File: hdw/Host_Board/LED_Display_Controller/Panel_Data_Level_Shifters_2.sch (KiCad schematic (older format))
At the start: 62 parts

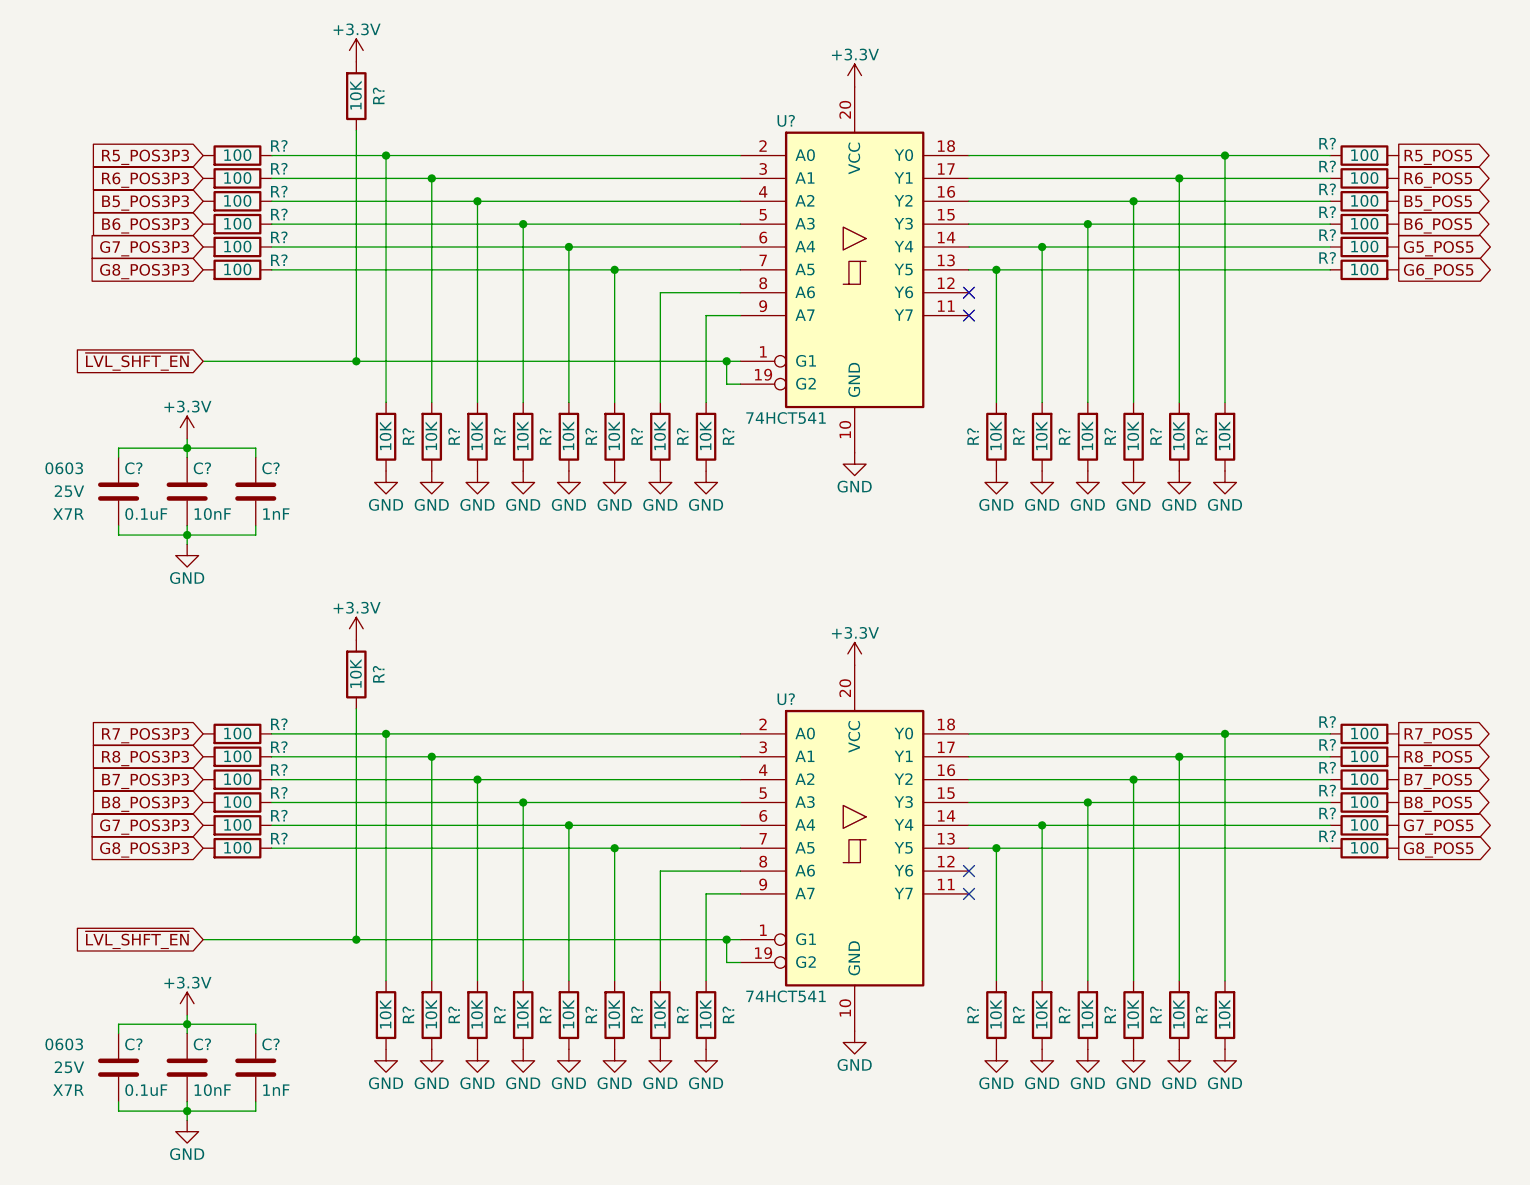
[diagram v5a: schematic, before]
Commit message: Added panel output enable AND gate
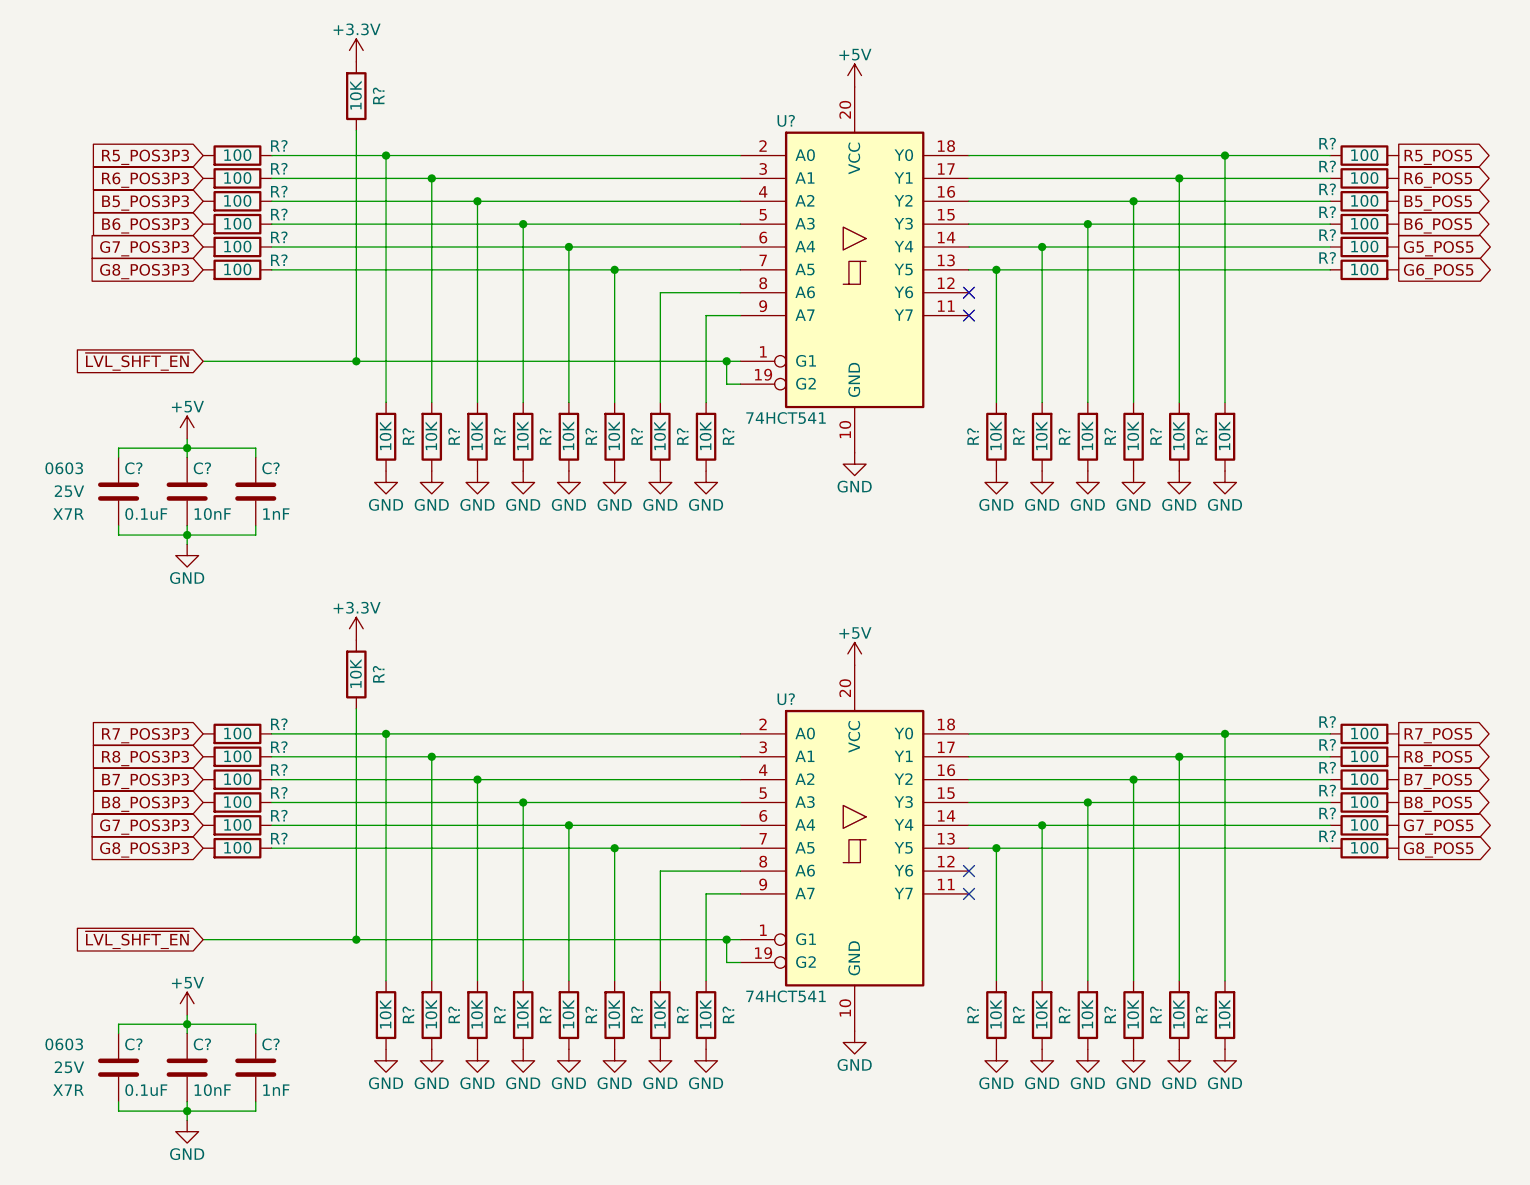
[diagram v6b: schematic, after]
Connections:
- net +3V3: no longer C?.1, C?.1, C?.1, C?.1, C?.1, C?.1, U?.20 (VCC), U?.20 (VCC)
- new net +5V: C?.1, C?.1, C?.1, C?.1, C?.1, C?.1, U?.20 (VCC), U?.20 (VCC)
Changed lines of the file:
@@
 $Descr A 11000 8500
 encoding utf-8
-Sheet 24 31
+Sheet 23 31
 Title ""
 Date ""
@@
 G6_POS5
 $Comp
-L power:+3.3V #PWR?
-U 1 1 5BB71AEA
-P 5500 1420
-AR Path="/5BAAE2B6/5BB71AEA" Ref="#PWR?"  Part="1"
-AR Path="/5BB6CF70/5BB71AEA" Ref="#PWR?"  Part="1"
-AR Path="/5BBE424F/5BB71AEA" Ref="#PWR?"  Part="1"
-F 0 "#PWR?" H 5500 1270 50  0001 C CNN
-F 1 "+3.3V" H 5500 1560 50  0000 C CNN
-F 2 "" H 5500 1420 50  0001 C CNN
-F 3 "" H 5500 1420 50  0001 C CNN
-	1    5500 1420
-	1    0    0    -1
-$EndComp
-$Comp
 L power:GND #PWR?
 U 1 1 5BB71AF0
@@
 G8_POS5
 $Comp
-L power:+3.3V #PWR?
-U 1 1 5BB71CCB
-P 5500 3950
-AR Path="/5BAAE2B6/5BB71CCB" Ref="#PWR?"  Part="1"
-AR Path="/5BB6CF70/5BB71CCB" Ref="#PWR?"  Part="1"
-AR Path="/5BBE424F/5BB71CCB" Ref="#PWR?"  Part="1"
-F 0 "#PWR?" H 5500 3800 50  0001 C CNN
-F 1 "+3.3V" H 5500 4090 50  0000 C CNN
-F 2 "" H 5500 3950 50  0001 C CNN
-F 3 "" H 5500 3950 50  0001 C CNN
-	1    5500 3950
-	1    0    0    -1
-$EndComp
-$Comp
 L power:GND #PWR?
 U 1 1 5BB71CD1
@@
 Wire Wire Line
 	2880 3380 2880 3340
-$Comp
-L power:+3.3V #PWR?
-U 1 1 5BB9D25C
-P 2580 2960
-AR Path="/5BAAE16C/5BB9D25C" Ref="#PWR?"  Part="1"
-AR Path="/5BB6CF70/5BB9D25C" Ref="#PWR?"  Part="1"
-AR Path="/5BBE424F/5BB9D25C" Ref="#PWR?"  Part="1"
-F 0 "#PWR?" H 2580 2810 50  0001 C CNN
-F 1 "+3.3V" H 2580 3100 50  0000 C CNN
-F 2 "" H 2580 2960 50  0001 C CNN
-F 3 "" H 2580 2960 50  0001 C CNN
-	1    2580 2960
-	1    0    0    -1
-$EndComp
 Wire Wire Line
 	2580 2960 2580 3000
@@
 Wire Wire Line
 	2880 5900 2880 5860
-$Comp
-L power:+3.3V #PWR?
-U 1 1 5BBD70FD
+Wire Wire Line
+	2580 5480 2580 5520
+Wire Wire Line
+	2280 5560 2280 5520
+Wire Wire Line
+	2280 5520 2580 5520
+Wire Wire Line
+	2880 5520 2880 5560
+Connection ~ 2580 5520
+Wire Wire Line
+	2580 5520 2580 5560
+Wire Wire Line
+	2580 5520 2880 5520
+$Comp
+L power:+5V #PWR?
+U 1 1 5BF4E41B
+P 5500 1420
+F 0 "#PWR?" H 5500 1270 50  0001 C CNN
+F 1 "+5V" H 5500 1560 50  0000 C CNN
+F 2 "" H 5500 1420 50  0001 C CNN
+F 3 "" H 5500 1420 50  0001 C CNN
+	1    5500 1420
+	1    0    0    -1
+$EndComp
+$Comp
+L power:+5V #PWR?
+U 1 1 5BF4E5A1
+P 2580 2960
+F 0 "#PWR?" H 2580 2810 50  0001 C CNN
+F 1 "+5V" H 2580 3100 50  0000 C CNN
+F 2 "" H 2580 2960 50  0001 C CNN
+F 3 "" H 2580 2960 50  0001 C CNN
+	1    2580 2960
+	1    0    0    -1
+$EndComp
+$Comp
+L power:+5V #PWR?
+U 1 1 5BF4E8D2
+P 5500 3950
+F 0 "#PWR?" H 5500 3800 50  0001 C CNN
+F 1 "+5V" H 5500 4090 50  0000 C CNN
+F 2 "" H 5500 3950 50  0001 C CNN
+F 3 "" H 5500 3950 50  0001 C CNN
+	1    5500 3950
+	1    0    0    -1
+$EndComp
+$Comp
+L power:+5V #PWR?
+U 1 1 5BF4ED50
 P 2580 5480
-AR Path="/5BAAE16C/5BBD70FD" Ref="#PWR?"  Part="1"
-AR Path="/5BB6CF70/5BBD70FD" Ref="#PWR?"  Part="1"
-AR Path="/5BBE424F/5BBD70FD" Ref="#PWR?"  Part="1"
 F 0 "#PWR?" H 2580 5330 50  0001 C CNN
-F 1 "+3.3V" H 2580 5620 50  0000 C CNN
+F 1 "+5V" H 2580 5620 50  0000 C CNN
 F 2 "" H 2580 5480 50  0001 C CNN
 F 3 "" H 2580 5480 50  0001 C CNN
@@
 	1    0    0    -1
 $EndComp
-Wire Wire Line
-	2580 5480 2580 5520
-Wire Wire Line
-	2280 5560 2280 5520
-Wire Wire Line
-	2280 5520 2580 5520
-Wire Wire Line
-	2880 5520 2880 5560
-Connection ~ 2580 5520
-Wire Wire Line
-	2580 5520 2580 5560
-Wire Wire Line
-	2580 5520 2880 5520
 $EndSCHEMATC

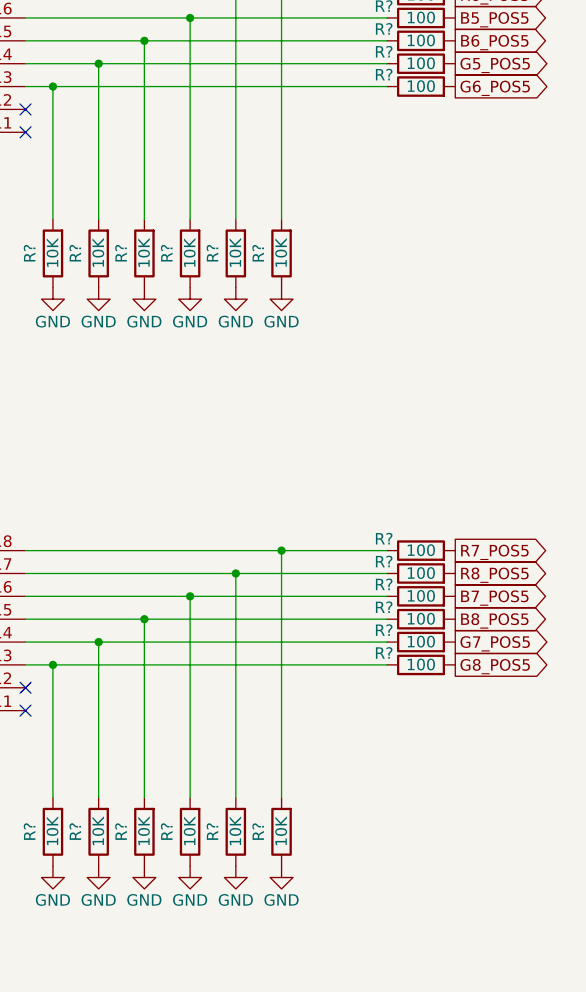
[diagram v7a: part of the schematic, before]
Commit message: Added graphical symbols to certain sheets
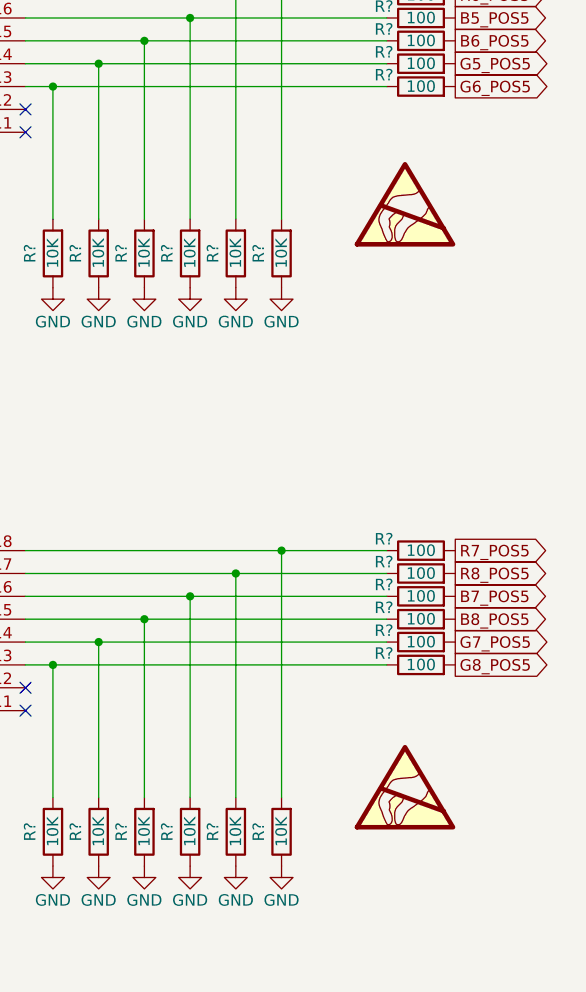
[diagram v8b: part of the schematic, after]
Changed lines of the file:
@@
+	1    0    0    -1
+$EndComp
+$Comp
+L Graphic:SYM_ESD_Large #SYM?
+U 1 1 5C041CF2
+P 7660 2710
+AR Path="/5BAAE0FA/5C041CF2" Ref="#SYM?"  Part="1"
+AR Path="/5BB182B1/5C041CF2" Ref="#SYM?"  Part="1"
+F 0 "#SYM?" H 7660 2910 50  0001 C CNN
+F 1 "SYM_ESD_Large" H 7660 2460 50  0001 C CNN
+F 2 "" H 7655 2680 50  0001 C CNN
+F 3 "~" H 7655 2680 50  0001 C CNN
+	1    7660 2710
+	1    0    0    -1
+$EndComp
+$Comp
+L Graphic:SYM_ESD_Large #SYM?
+U 1 1 5C045E39
+P 7660 5260
+AR Path="/5BAAE0FA/5C045E39" Ref="#SYM?"  Part="1"
+AR Path="/5BB182B1/5C045E39" Ref="#SYM?"  Part="1"
+F 0 "#SYM?" H 7660 5460 50  0001 C CNN
+F 1 "SYM_ESD_Large" H 7660 5010 50  0001 C CNN
+F 2 "" H 7655 5230 50  0001 C CNN
+F 3 "~" H 7655 5230 50  0001 C CNN
+	1    7660 5260
 	1    0    0    -1
 $EndComp
